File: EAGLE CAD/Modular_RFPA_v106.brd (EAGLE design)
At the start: 152.4 x 152.4 mm, 197 parts, among them IC301 74AHC1G14DBV, IC302 LM324D, J401 FUSE_2P, J402 KK_PCFAN, Q101 IRF520N, Q102 IRF630, Q201 IRF630, Q202 IRF630, Q301 BSS123, T101 HP4_TRAFO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

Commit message: copy "R" variants to "R90"
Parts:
- R401: value (none) -> 1K; device resistor:P0817V -> MDT_R:R1206
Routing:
- net N$44: track 18.0 -> 21.7 mm
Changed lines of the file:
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@@
 <element name="IC402" library="v-reg" package="78XXS" value="" x="101.6" y="60.96" rot="R180"/>
 <element name="D401" library="diode" package="SMC" value="" x="127.762" y="31.242" rot="R270"/>
-<element name="R401" library="resistor" package="P0817V" value="" x="138.43" y="46.99" rot="R90"/>
+<element name="R401" library="MDT_R" package="R1206" value="1K" x="138.43" y="46.99" rot="R90">
+<attribute name="PACKAGE" value="1206" x="138.43" y="46.99" size="1.778" layer="27" rot="R90" display="off"/>
+<attribute name="PARTNO" value="" x="138.43" y="46.99" size="1.778" layer="27" rot="R90" display="off"/>
+<attribute name="BOM" value="" x="138.43" y="46.99" size="1.778" layer="27" rot="R90" display="off"/>
+<attribute name="TOL" value="1%" x="138.43" y="46.99" size="1.778" layer="27" rot="R90" display="off"/>
+<attribute name="VALUE" value="1K" x="138.43" y="46.99" size="1.778" layer="27" rot="R90" display="off"/>
+<attribute name="POWER" value="0.25" x="138.43" y="46.99" size="1.778" layer="27" rot="R90" display="off"/>
+</element>
 <element name="C401" library="rcl" package="EB25D" value="3300uF" x="135.89" y="63.5" rot="R180"/>
 <element name="C405" library="MDT_C" package="C2220_CKG57N" value="10uF" x="113.538" y="121.92" rot="R270">
@@
 <contactref element="R401" pad="1"/>
 <contactref element="J401" pad="2"/>
-<wire x1="138.43" y1="34.671" x2="138.43" y2="41.91" width="1.778" layer="1"/>
+<wire x1="138.43" y1="34.671" x2="138.43" y2="45.568" width="1.778" layer="1"/>
 <wire x1="138.43" y1="34.671" x2="128.033" y2="34.671" width="1.778" layer="1"/>
 <wire x1="128.033" y1="34.671" x2="127.762" y2="34.942" width="1.778" layer="1"/>
@@
 <contactref element="C401" pad="+"/>
 <contactref element="L401" pad="1"/>
-<wire x1="138.43" y1="48.26" x2="140.97" y2="50.8" width="2.54" layer="1"/>
+<wire x1="138.43" y1="48.412" x2="140.97" y2="50.8" width="2.54" layer="1"/>
 <wire x1="140.97" y1="50.8" x2="140.97" y2="63.5" width="2.54" layer="1"/>
 <wire x1="140.97" y1="63.5" x2="140.97" y2="91.948" width="2.54" layer="1"/>

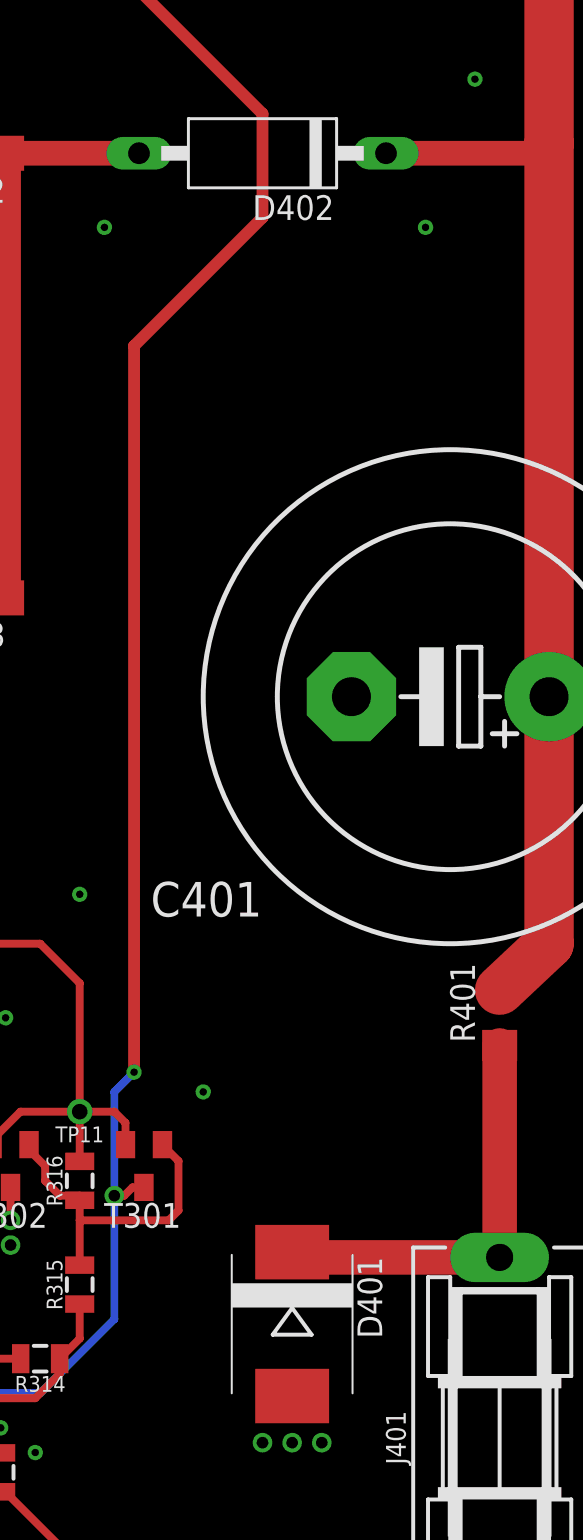
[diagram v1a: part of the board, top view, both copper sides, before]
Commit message: More schematic/library changes
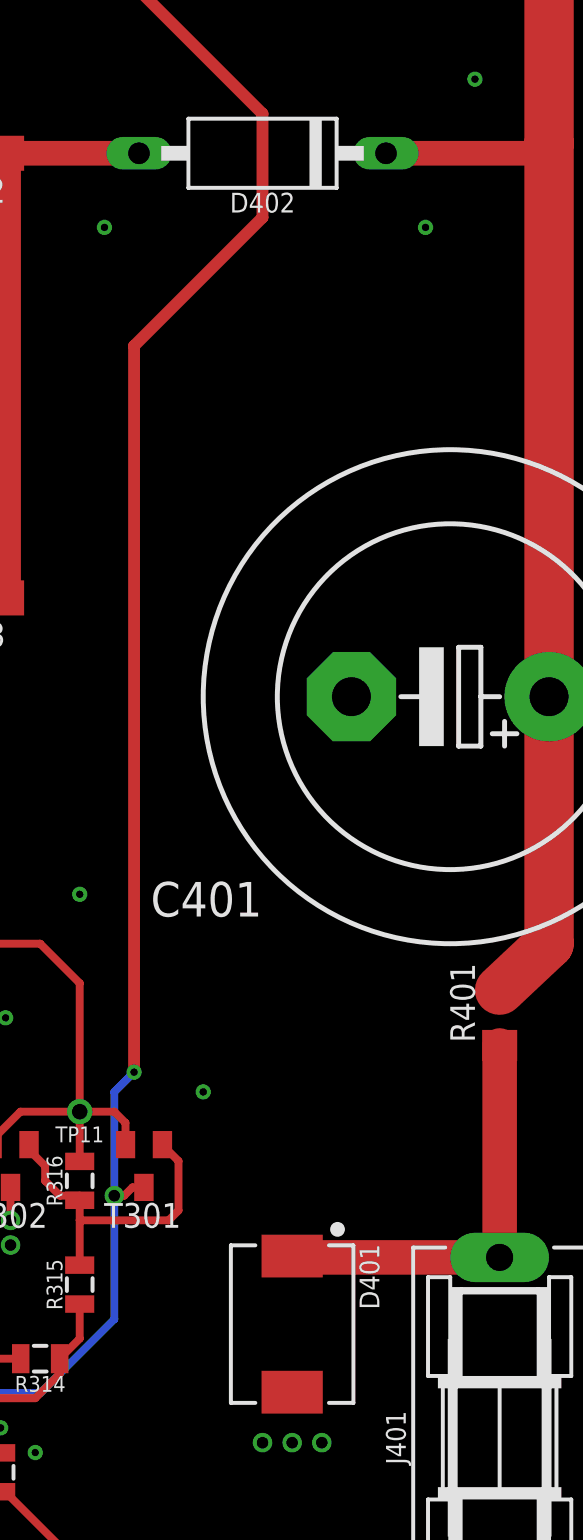
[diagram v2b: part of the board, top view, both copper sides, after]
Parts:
- D401: value (none) -> D-SCHOTTKYSK810L-TPSMC; device diode:SMC -> MDT_Diode:DO-214AB(SMC)
- D402: value GP15 -> D-ZENER1N5355B-TPDO15-12; device diode:DO15-12 -> MDT_Diode:DO15-12
- R401, R402, R403, R404: value 1K -> 1.0
- R405: value 1K -> 0.5
- R406: value 1.0K -> 2K
- R407: value 1.0K -> 590
- R408: value 1.0K -> 10K
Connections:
- net N$44: now also D401.K; no longer D401.C

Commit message: .
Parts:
- R401: device MDT_R:R1206 -> resistor:P0817V
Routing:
- net DRAINS_POS: track 117.1 -> 125.7 mm
- net DRAINS_NEG: track 128.3 -> 136.9 mm
- net +5V: track 153.5 -> 159.8 mm
- net +12V: track 137.4 -> 143.7 mm
- net N$44: track 21.6 -> 17.9 mm
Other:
- board text added: "EASY RFPA FAB"
- board text removed: "DIY RFPA MODULE"
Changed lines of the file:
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@@
 <layer number="25" name="tNames" color="7" fill="1" visible="yes" active="yes"/>
 <layer number="26" name="bNames" color="7" fill="1" visible="yes" active="yes"/>
-<layer number="27" name="tValues" color="7" fill="1" visible="no" active="yes"/>
-<layer number="28" name="bValues" color="7" fill="1" visible="no" active="yes"/>
+<layer number="27" name="tValues" color="7" fill="1" visible="yes" active="yes"/>
+<layer number="28" name="bValues" color="7" fill="1" visible="yes" active="yes"/>
 <layer number="29" name="tStop" color="7" fill="3" visible="yes" active="yes"/>
 <layer number="30" name="bStop" color="7" fill="6" visible="yes" active="yes"/>
@@
 <wire x1="152.4" y1="152.4" x2="0" y2="152.4" width="0.3048" layer="20"/>
 <wire x1="0" y1="152.4" x2="0" y2="0" width="0.3048" layer="20"/>
-<text x="2.54" y="15.24" size="1.778" layer="1" font="vector" ratio="15">DIY RFPA MODULE</text>
+<text x="2.54" y="15.24" size="1.778" layer="1" font="vector" ratio="15">EASY RFPA FAB</text>
 <text x="2.54" y="10.16" size="1.778" layer="1" font="vector" ratio="15">Mike Twieg 2022036</text>
 <text x="2.54" y="12.7" size="1.778" layer="1" font="vector" ratio="15">Rev A</text>
@@
 </attributes>
 <variantdefs>
-<variantdef name="IRF520N_20W" current="yes"/>
+<variantdef name="IRF520N_20W"/>
 <variantdef name="IRF630_200W"/>
 </variantdefs>
@@
 <attribute name="BOM" value="INCLUDE" x="127.762" y="31.242" size="1.778" layer="27" rot="R270" display="off"/>
 </element>
-<element name="R401" library="MDT_R" package="R1206" value="1.0" x="138.43" y="46.99" rot="R90">
-<attribute name="PACKAGE" value="1206" x="138.43" y="46.99" size="1.778" layer="27" rot="R90" display="off"/>
-<attribute name="PARTNO" value="" x="138.43" y="46.99" size="1.778" layer="27" rot="R90" display="off"/>
-<attribute name="BOM" value="" x="138.43" y="46.99" size="1.778" layer="27" rot="R90" display="off"/>
-<attribute name="TOL" value="1%" x="138.43" y="46.99" size="1.778" layer="27" rot="R90" display="off"/>
-<attribute name="VALUE" value="1K" x="138.43" y="46.99" size="1.778" layer="27" rot="R90" display="off"/>
-<attribute name="POWER" value="0.25" x="138.43" y="46.99" size="1.778" layer="27" rot="R90" display="off"/>
-</element>
+<element name="R401" library="resistor" package="P0817V" value="1.0" x="138.43" y="46.99" rot="R90"/>
 <element name="C401" library="rcl" package="EB25D" value="3300uF" x="135.89" y="63.5" rot="R180"/>
 <element name="C405" library="MDT_C" package="C2220_CKG57N" value="10uF" x="113.538" y="121.92" rot="R270">
@@
 <element name="C409" library="rcl" package="E2,5-7" value="22uF" x="98.806" y="97.79"/>
 <element name="L103" library="MDT_L" package="DR127" value="" x="26.67" y="121.92" rot="R90">
-<attribute name="ESR" value="39.1m" x="26.67" y="121.92" size="1.778" layer="27" rot="R90" display="off"/>
-<attribute name="CURRENT" value="4.0A" x="26.67" y="121.92" size="1.778" layer="27" rot="R90" display="off"/>
-<attribute name="PARTNO" value="DR127-220-R" x="26.67" y="121.92" size="1.778" layer="27" rot="R90" display="off"/>
-<attribute name="DEVICE" value="DR127-220-R" x="26.67" y="121.92" size="1.778" layer="27" rot="R90" display="off"/>
-<attribute name="BOM" value="INCLUDE" x="26.67" y="121.92" size="1.778" layer="27" rot="R90" display="off"/>
-<attribute name="TOL" value="20%" x="26.67" y="121.92" size="1.778" layer="27" rot="R90" display="off"/>
-<attribute name="VALUE" value="22uH" x="26.67" y="121.92" size="1.778" layer="27" rot="R90" display="off"/>
+<attribute name="ESR" value="" x="26.67" y="121.92" size="1.778" layer="27" rot="R90" display="off"/>
+<attribute name="CURRENT" value="" x="26.67" y="121.92" size="1.778" layer="27" rot="R90" display="off"/>
+<attribute name="PARTNO" value="" x="26.67" y="121.92" size="1.778" layer="27" rot="R90" display="off"/>
+<attribute name="DEVICE" value="" x="26.67" y="121.92" size="1.778" layer="27" rot="R90" display="off"/>
+<attribute name="BOM" value="" x="26.67" y="121.92" size="1.778" layer="27" rot="R90" display="off"/>
+<attribute name="TOL" value="" x="26.67" y="121.92" size="1.778" layer="27" rot="R90" display="off"/>
+<attribute name="VALUE" value="" x="26.67" y="121.92" size="1.778" layer="27" rot="R90" display="off"/>
 <variant name="IRF520N_20W" value="22uH"/>
 <variant name="IRF630_200W" value="3.3uH"/>
 </element>
 <element name="L104" library="MDT_L" package="DR127" value="" x="74.93" y="121.92" rot="R90">
-<attribute name="ESR" value="39.1m" x="74.93" y="121.92" size="1.778" layer="27" rot="R90" display="off"/>
-<attribute name="CURRENT" value="4.0A" x="74.93" y="121.92" size="1.778" layer="27" rot="R90" display="off"/>
-<attribute name="PARTNO" value="DR127-220-R" x="74.93" y="121.92" size="1.778" layer="27" rot="R90" display="off"/>
-<attribute name="DEVICE" value="DR127-220-R" x="74.93" y="121.92" size="1.778" layer="27" rot="R90" display="off"/>
-<attribute name="BOM" value="INCLUDE" x="74.93" y="121.92" size="1.778" layer="27" rot="R90" display="off"/>
-<attribute name="TOL" value="20%" x="74.93" y="121.92" size="1.778" layer="27" rot="R90" display="off"/>
-<attribute name="VALUE" value="22uH" x="74.93" y="121.92" size="1.778" layer="27" rot="R90" display="off"/>
+<attribute name="ESR" value="" x="74.93" y="121.92" size="1.778" layer="27" rot="R90" display="off"/>
+<attribute name="CURRENT" value="" x="74.93" y="121.92" size="1.778" layer="27" rot="R90" display="off"/>
+<attribute name="PARTNO" value="" x="74.93" y="121.92" size="1.778" layer="27" rot="R90" display="off"/>
+<attribute name="DEVICE" value="" x="74.93" y="121.92" size="1.778" layer="27" rot="R90" display="off"/>
+<attribute name="BOM" value="" x="74.93" y="121.92" size="1.778" layer="27" rot="R90" display="off"/>
+<attribute name="TOL" value="" x="74.93" y="121.92" size="1.778" layer="27" rot="R90" display="off"/>
+<attribute name="VALUE" value="" x="74.93" y="121.92" size="1.778" layer="27" rot="R90" display="off"/>
 <variant name="IRF520N_20W" value="22uH"/>
 <variant name="IRF630_200W" value="3.3uH"/>
@@
 <wire x1="104.088" y1="99.77" x2="119.94" y2="99.77" width="0.6096" layer="1"/>
 <contactref element="LED401" pad="A"/>
-<wire x1="97.66" y1="87.76" x2="92.71" y2="86.36" width="0" layer="19" extent="1-1"/>
+<wire x1="92.71" y1="86.36" x2="99.06" y2="86.36" width="0.4064" layer="16"/>
 </signal>
 <signal name="N$3">
@@
 <wire x1="53.34" y1="50.546" x2="53.34" y2="57.15" width="0.8128" layer="1"/>
 <contactref element="L104" pad="1"/>
-<wire x1="74.93" y1="116.945" x2="83.335" y2="116.945" width="0" layer="19" extent="1-1"/>
-<wire x1="74.825" y1="116.84" x2="74.93" y2="116.945" width="0" layer="19" extent="1-1"/>
+<wire x1="83.335" y1="116.945" x2="74.93" y2="116.945" width="0.8128" layer="1"/>
+<wire x1="74.825" y1="116.84" x2="74.93" y2="116.84" width="0.4064" layer="1"/>
+<wire x1="74.93" y1="116.84" x2="74.93" y2="116.945" width="0.4064" layer="1"/>
 </signal>
 <signal name="BN5">
@@
 <wire x1="97.536" y1="76.2" x2="95.504" y2="76.2" width="0.6096" layer="1"/>
 <contactref element="LED402" pad="A"/>
-<wire x1="97.66" y1="64.9" x2="92.71" y2="63.5" width="0" layer="19" extent="1-1"/>
+<wire x1="92.71" y1="63.5" x2="99.06" y2="63.5" width="0.4064" layer="1"/>
 </signal>
 <signal name="N$43">
@@
 <contactref element="R401" pad="1"/>
 <contactref element="J401" pad="2"/>
-<wire x1="138.43" y1="34.671" x2="138.43" y2="45.568" width="1.778" layer="1"/>
+<wire x1="138.43" y1="34.671" x2="138.43" y2="41.91" width="1.778" layer="1"/>
 <wire x1="138.43" y1="34.671" x2="128.033" y2="34.671" width="1.778" layer="1"/>
 <wire x1="128.033" y1="34.671" x2="127.762" y2="34.742" width="1.778" layer="1"/>
@@
 <contactref element="C401" pad="+"/>
 <contactref element="L401" pad="1"/>
-<wire x1="138.43" y1="48.412" x2="140.97" y2="50.8" width="2.54" layer="1"/>
+<wire x1="138.43" y1="48.26" x2="140.97" y2="50.8" width="2.54" layer="1"/>
 <wire x1="140.97" y1="50.8" x2="140.97" y2="63.5" width="2.54" layer="1"/>
 <wire x1="140.97" y1="63.5" x2="140.97" y2="91.948" width="2.54" layer="1"/>
@@
 <wire x1="47.882" y1="66.418" x2="48.26" y2="66.04" width="0.8128" layer="1"/>
 <contactref element="L103" pad="1"/>
-<wire x1="26.775" y1="116.84" x2="26.67" y2="116.945" width="0" layer="19" extent="1-1"/>
-<wire x1="18.265" y1="116.945" x2="26.67" y2="116.945" width="0" layer="19" extent="1-1"/>
+<wire x1="18.265" y1="116.945" x2="26.67" y2="116.945" width="0.8128" layer="1"/>
+<wire x1="26.775" y1="116.84" x2="26.67" y2="116.84" width="0.4064" layer="1"/>
+<wire x1="26.67" y1="116.84" x2="26.67" y2="116.945" width="0.4064" layer="1"/>
 </signal>
 <signal name="BP2">
